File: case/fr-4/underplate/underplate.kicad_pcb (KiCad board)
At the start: 2 copper layers, 152.4 x 104.6 mm, 5 parts

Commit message: Fill all zones
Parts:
- added H6: Hole_Mount_M2, jiran-ble-lite:Hole_Mount_M2, F.Cu at (206.6, 106.2)
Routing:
- added copper zone on B.Cu, net (none)
- added copper zone on F.Cu, net (none)
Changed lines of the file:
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@@
       (drillshape 0)
       (scaleselection 1)
-      (outputdirectory "gerbers/")
+      (outputdirectory "D:/Git/jiran-ble-lite/case/fr-4/underplate/gerbers/")
     )
   )
   (net 0 "")
+  (footprint "jiran-ble-lite:Hole_Mount_M2" (layer "F.Cu")
+    (at 206.5782 106.2228)
+    (fp_text reference "H6" (at 0 0 unlocked) (layer "F.SilkS") hide
+      (effects (font (size 1 1) (thickness 0.15)))
+    )
+    (fp_text value "Hole_Mount_M2" (at 0 2.65 unlocked) (layer "F.Fab") hide
+      (effects (font (size 1 1) (thickness 0.15)))
+    )
+    (fp_circle (center 0 0) (end 1.5 0) (layer "Cmts.User") (width 0.12) (fill none))
+    (pad "" np_thru_hole circle (at 0 0) (size 2.1 2.1) (drill 2.1) (layers *.Cu *.Mask))
+  )
   (footprint "jiran-ble-lite:Hole_Mount_M2" (layer "F.Cu")
     (at 107.696 74.93)
@@
   (gr_arc (start 220.853 146.304) (end 220.853 147.447) (angle -90) (layer "Edge.Cuts") (width 0.1))
   (gr_arc (start 88.011 99.314) (end 87.376004 99.314) (angle 90) (layer "Edge.Cuts") (width 0.1))
+  (gr_line (start 204.089 147.447) (end 220.853 147.447) (layer "Edge.Cuts") (width 0.1))
   (gr_arc (start 127.889 48.768) (end 127.889 47.625) (angle -90) (layer "Edge.Cuts") (width 0.1))
   (gr_arc (start 106.553 55.88) (end 106.553 57.023) (angle -90) (layer "Edge.Cuts") (width 0.1))
@@
   (gr_arc (start 88.011 105.918004) (end 88.645996 105.918004) (angle 90) (layer "Edge.Cuts") (width 0.1))
   (gr_arc (start 201.803 146.304) (end 202.946 146.304) (angle -90) (layer "Edge.Cuts") (width 0.1))
-  (gr_line (start 220.853 147.447) (end 204.089 147.447) (layer "Edge.Cuts") (width 0.1))
   (gr_line (start 221.996 146.304) (end 221.996 54.864) (layer "Edge.Cuts") (width 0.1))
   (gr_line (start 108.839 54.737) (end 125.603 54.737) (layer "Edge.Cuts") (width 0.1))
   (gr_arc (start 125.603 129.794) (end 125.603 130.937) (angle -90) (layer "Edge.Cuts") (width 0.1))
   (gr_line (start 201.803 145.161) (end 185.039 145.161) (layer "Edge.Cuts") (width 0.1))
+  (zone (net 0) (net_name "") (layer "F.Cu") (hatch edge 0.508)
+    (connect_pads (clearance 0.508))
+    (min_thickness 0.254) (filled_areas_thickness no)
+    (fill yes (thermal_gap 0.508) (thermal_bridge_width 0.508))
+    (polygon
+      (pts
+        (xy 164.846 47.625)
+        (xy 183.896 47.625)
+        (xy 183.896 49.911)
+        (xy 202.946 49.911)
+        (xy 202.946 53.721)
+        (xy 221.996 53.721)
+        (xy 221.996 147.447)
+        (xy 202.946 147.447)
+        (xy 202.946 145.161)
+        (xy 183.896 145.161)
+        (xy 183.896 142.875)
+        (xy 164.846 142.875)
+        (xy 164.846 118.999)
+        (xy 145.796 118.999)
+        (xy 145.796 123.825)
+        (xy 126.746 123.825)
+        (xy 126.746 130.937)
+        (xy 107.696 130.937)
+        (xy 107.696 133.223)
+        (xy 88.646 133.223)
+        (xy 88.646 109.347)
+        (xy 69.596 109.347)
+        (xy 69.596 90.297)
+        (xy 88.646 90.297)
+        (xy 88.646 57.023)
+        (xy 107.696 57.023)
+        (xy 107.696 54.737)
+        (xy 126.746 54.737)
+        (xy 126.746 47.625)
+        (xy 145.796 47.625)
+        (xy 145.796 42.799)
+        (xy 164.846 42.799)
+      )
+    )
+  )
+  (zone (net 0) (net_name "") (layer "B.Cu") (hatch edge 0.508)
+    (connect_pads (clearance 0.508))
+    (min_thickness 0.254) (filled_areas_thickness no)
+    (fill yes (thermal_gap 0.508) (thermal_bridge_width 0.508))
+    (polygon
+      (pts
+        (xy 164.846 47.625)
+        (xy 183.896 47.625)
+        (xy 183.896 49.911)
+        (xy 202.946 49.911)
+        (xy 202.946 53.721)
+        (xy 221.996 53.721)
+        (xy 221.996 147.447)
+        (xy 202.946 147.447)
+        (xy 202.946 145.161)
+        (xy 183.896 145.161)
+        (xy 183.896 142.875)
+        (xy 164.846 142.875)
+        (xy 164.846 118.999)
+        (xy 145.796 118.999)
+        (xy 145.796 123.825)
+        (xy 126.746 123.825)
+        (xy 126.746 130.937)
+        (xy 107.696 130.937)
+        (xy 107.696 133.223)
+        (xy 88.646 133.223)
+        (xy 88.646 109.347)
+        (xy 69.596 109.347)
+        (xy 69.596 90.297)
+        (xy 88.646 90.297)
+        (xy 88.646 57.023)
+        (xy 107.696 57.023)
+        (xy 107.696 54.737)
+        (xy 126.746 54.737)
+        (xy 126.746 47.625)
+        (xy 145.796 47.625)
+        (xy 145.796 42.799)
+        (xy 164.846 42.799)
+      )
+    )
+  )
 )

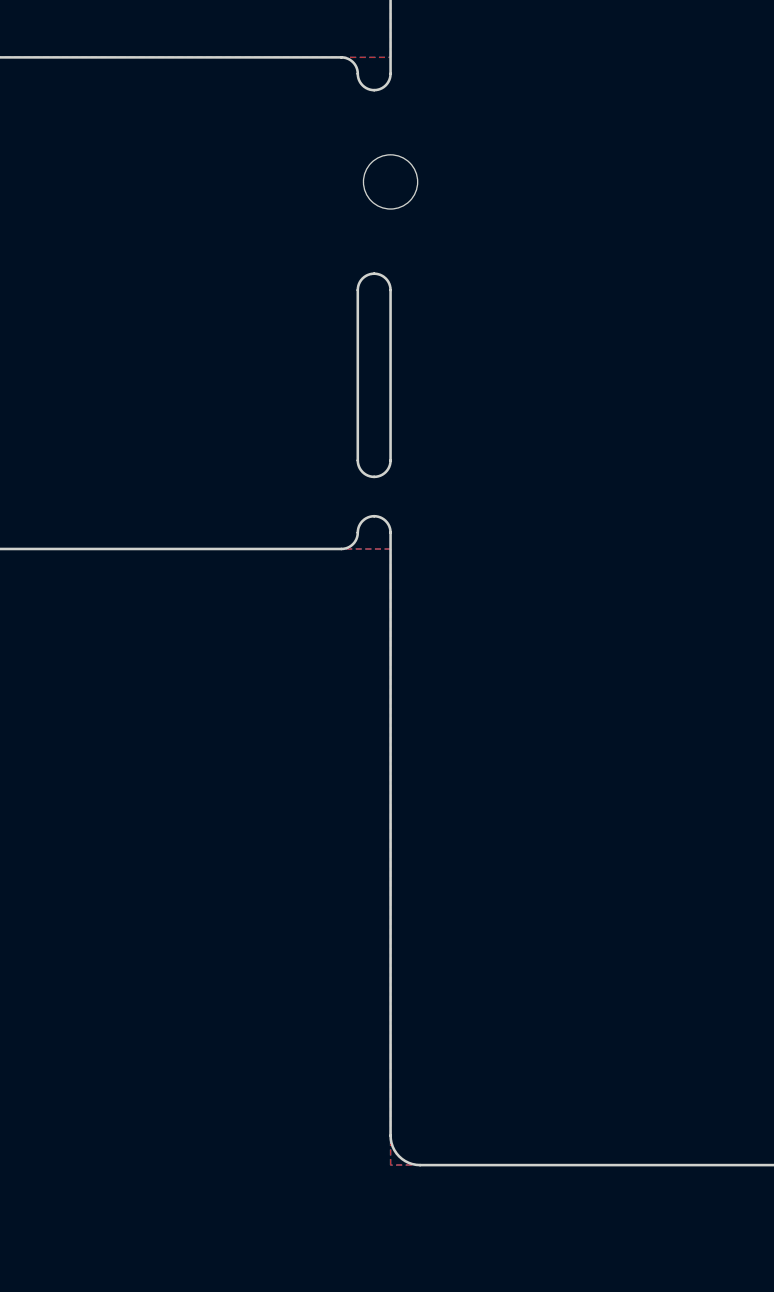
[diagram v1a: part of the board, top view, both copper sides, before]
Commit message: Edit cutout, re-fill zones
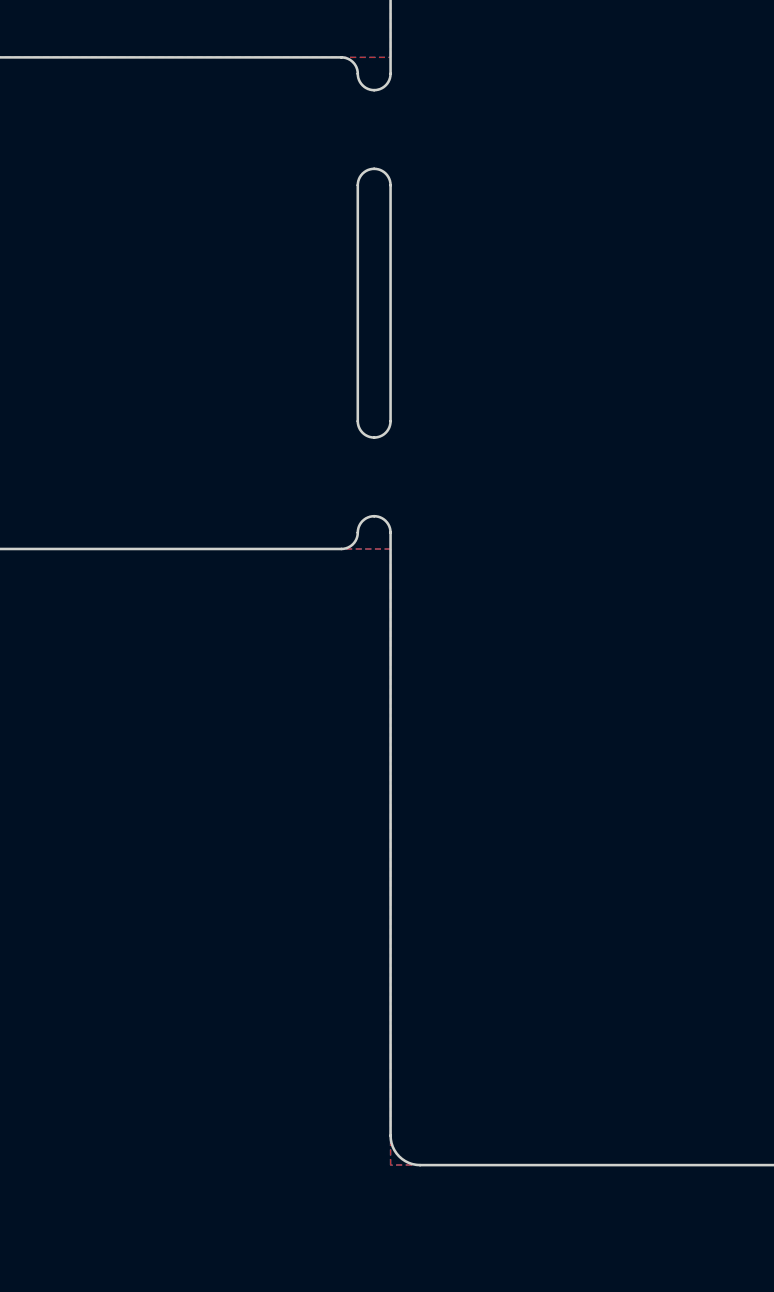
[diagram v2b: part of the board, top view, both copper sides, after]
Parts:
- removed H5: Hole_Mount_M2, jiran-ble-lite:Hole_Mount_M2
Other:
- outline, holes or cut-outs redrawn
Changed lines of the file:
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@@
-  )
-  (footprint "jiran-ble-lite:Hole_Mount_M2" (layer "F.Cu")
-    (at 88.646 95.123)
-    (fp_text reference "H5" (at 0 0 unlocked) (layer "F.SilkS") hide
-      (effects (font (size 1 1) (thickness 0.15)))
-    )
-    (fp_text value "Hole_Mount_M2" (at 0 2.65 unlocked) (layer "F.Fab") hide
-      (effects (font (size 1 1) (thickness 0.15)))
-    )
-    (fp_circle (center 0 0) (end 1.5 0) (layer "Cmts.User") (width 0.12) (fill none))
-    (pad "" np_thru_hole circle (at 0 0) (size 2.1 2.1) (drill 2.1) (layers *.Cu *.Mask))
   )
   (footprint "jiran-ble-lite:Hole_Mount_M2" (layer "F.Cu")
@@
     (pad "" np_thru_hole circle (at 0 0) (size 2.1 2.1) (drill 2.1) (layers *.Cu *.Mask))
   )
-  (gr_line (start 88.645996 105.918004) (end 88.645996 99.314) (layer "Edge.Cuts") (width 0.1))
   (gr_line (start 145.796 120.142) (end 145.796 122.682) (layer "Edge.Cuts") (width 0.1))
   (gr_line (start 145.796 46.482) (end 145.796 43.942) (layer "Edge.Cuts") (width 0.1))
-  (gr_arc (start 88.010993 90.931999) (end 88.645989 90.931999) (angle 90) (layer "Edge.Cuts") (width 0.1))
   (gr_arc (start 89.789 132.08) (end 88.646 132.08) (angle -90) (layer "Edge.Cuts") (width 0.1))
   (gr_line (start 127.889 47.625) (end 144.653 47.625) (layer "Edge.Cuts") (width 0.1))
   (gr_arc (start 165.989 141.732) (end 164.846 141.732) (angle -90) (layer "Edge.Cuts") (width 0.1))
-  (gr_line (start 88.646 58.166) (end 88.645989 90.931999) (layer "Edge.Cuts") (width 0.1))
+  (gr_line (start 88.645996 104.394004) (end 88.645996 95.249996) (layer "Edge.Cuts") (width 0.1))
   (gr_arc (start 185.039 144.018) (end 183.896 144.018) (angle -90) (layer "Edge.Cuts") (width 0.1))
   (gr_arc (start 146.939 43.942) (end 146.939 42.799) (angle -90) (layer "Edge.Cuts") (width 0.1))
   (gr_line (start 182.753 142.875) (end 165.989 142.875) (layer "Edge.Cuts") (width 0.1))
+  (gr_line (start 88.646 58.166) (end 88.645989 90.931999) (layer "Edge.Cuts") (width 0.1))
   (gr_line (start 202.946 51.054) (end 202.946 52.578) (layer "Edge.Cuts") (width 0.1))
-  (gr_arc (start 86.741 90.932) (end 86.741 90.297004) (angle 90) (layer "Edge.Cuts") (width 0.1))
   (gr_arc (start 163.703 43.942) (end 164.846 43.942) (angle -90) (layer "Edge.Cuts") (width 0.1))
   (gr_arc (start 127.889 124.968) (end 127.889 123.825) (angle -90) (layer "Edge.Cuts") (width 0.1))
   (gr_line (start 146.939 42.799) (end 163.703 42.799) (layer "Edge.Cuts") (width 0.1))
+  (gr_arc (start 88.010992 108.712004) (end 87.375996 108.712004) (angle 90) (layer "Edge.Cuts") (width 0.1))
   (gr_arc (start 220.853 54.864) (end 221.996 54.864) (angle -90) (layer "Edge.Cuts") (width 0.1))
   (gr_arc (start 182.753 48.768) (end 183.896 48.768) (angle -90) (layer "Edge.Cuts") (width 0.1))
@@
   (gr_line (start 70.739 90.297) (end 86.741 90.297004) (layer "Edge.Cuts") (width 0.1))
   (gr_arc (start 89.789 58.166) (end 89.789 57.023) (angle -90) (layer "Edge.Cuts") (width 0.1))
+  (gr_arc (start 86.741 108.712004) (end 87.375996 108.712004) (angle 90) (layer "Edge.Cuts") (width 0.1))
   (gr_line (start 164.846 141.732) (end 164.846 120.142) (layer "Edge.Cuts") (width 0.1))
   (gr_line (start 163.703 118.999) (end 146.939 118.999) (layer "Edge.Cuts") (width 0.1))
-  (gr_arc (start 88.010992 108.712004) (end 87.375996 108.712004) (angle 90) (layer "Edge.Cuts") (width 0.1))
+  (gr_line (start 87.376004 95.249996) (end 87.376004 104.394004) (layer "Edge.Cuts") (width 0.1))
+  (gr_arc (start 88.011 95.249996) (end 88.011 94.615) (angle 90) (layer "Edge.Cuts") (width 0.1))
   (gr_arc (start 220.853 146.304) (end 220.853 147.447) (angle -90) (layer "Edge.Cuts") (width 0.1))
-  (gr_arc (start 88.011 99.314) (end 87.376004 99.314) (angle 90) (layer "Edge.Cuts") (width 0.1))
+  (gr_arc (start 88.011 104.394004) (end 88.011 105.029) (angle 90) (layer "Edge.Cuts") (width 0.1))
   (gr_line (start 204.089 147.447) (end 220.853 147.447) (layer "Edge.Cuts") (width 0.1))
   (gr_arc (start 127.889 48.768) (end 127.889 47.625) (angle -90) (layer "Edge.Cuts") (width 0.1))
@@
   (gr_line (start 164.846 43.942) (end 164.846 46.482) (layer "Edge.Cuts") (width 0.1))
   (gr_line (start 165.989 47.625) (end 182.753 47.625) (layer "Edge.Cuts") (width 0.1))
+  (gr_arc (start 86.741 90.932) (end 86.741 90.297004) (angle 90) (layer "Edge.Cuts") (width 0.1))
+  (gr_line (start 88.645988 108.712004) (end 88.646 132.08) (layer "Edge.Cuts") (width 0.1))
   (gr_arc (start 165.989 46.482) (end 164.846 46.482) (angle -90) (layer "Edge.Cuts") (width 0.1))
-  (gr_arc (start 88.011 105.918004) (end 88.011 106.553) (angle 90) (layer "Edge.Cuts") (width 0.1))
+  (gr_arc (start 88.011 95.249996) (end 87.376004 95.249996) (angle 90) (layer "Edge.Cuts") (width 0.1))
+  (gr_arc (start 88.010992 108.712004) (end 88.010992 108.077008) (angle 90) (layer "Edge.Cuts") (width 0.1))
   (gr_arc (start 108.839 55.88) (end 108.839 54.737) (angle -90) (layer "Edge.Cuts") (width 0.1))
-  (gr_line (start 87.376004 99.314) (end 87.376004 105.918004) (layer "Edge.Cuts") (width 0.1))
   (gr_line (start 125.603 130.937) (end 108.839 130.937) (layer "Edge.Cuts") (width 0.1))
-  (gr_arc (start 88.011 99.314) (end 88.011 98.679004) (angle 90) (layer "Edge.Cuts") (width 0.1))
   (gr_line (start 69.596 108.204) (end 69.596 91.44) (layer "Edge.Cuts") (width 0.1))
   (gr_line (start 126.746 53.594) (end 126.746 48.768) (layer "Edge.Cuts") (width 0.1))
   (gr_arc (start 70.739 91.44) (end 70.739 90.297) (angle -90) (layer "Edge.Cuts") (width 0.1))
   (gr_line (start 144.653 123.825) (end 127.889 123.825) (layer "Edge.Cuts") (width 0.1))
-  (gr_arc (start 86.741 108.712004) (end 87.375996 108.712004) (angle 90) (layer "Edge.Cuts") (width 0.1))
-  (gr_line (start 88.646 132.08) (end 88.645987 108.712005) (layer "Edge.Cuts") (width 0.1))
   (gr_arc (start 201.803 51.054) (end 202.946 51.054) (angle -90) (layer "Edge.Cuts") (width 0.1))
   (gr_arc (start 70.739 108.204) (end 69.596 108.204) (angle -90) (layer "Edge.Cuts") (width 0.1))
@@
   (gr_line (start 106.553 133.223) (end 89.789 133.223) (layer "Edge.Cuts") (width 0.1))
   (gr_arc (start 204.089 146.304) (end 202.946 146.304) (angle -90) (layer "Edge.Cuts") (width 0.1))
-  (gr_arc (start 88.010991 108.712005) (end 88.010991 108.077009) (angle 90) (layer "Edge.Cuts") (width 0.1))
   (gr_arc (start 125.603 53.594) (end 125.603 54.737) (angle -90) (layer "Edge.Cuts") (width 0.1))
+  (gr_arc (start 88.010992 90.932) (end 88.010992 91.566996) (angle 90) (layer "Edge.Cuts") (width 0.1))
   (gr_arc (start 106.553 132.08) (end 106.553 133.223) (angle -90) (layer "Edge.Cuts") (width 0.1))
   (gr_arc (start 144.653 46.482) (end 144.653 47.625) (angle -90) (layer "Edge.Cuts") (width 0.1))
@@
   (gr_arc (start 144.653 122.682) (end 144.653 123.825) (angle -90) (layer "Edge.Cuts") (width 0.1))
   (gr_arc (start 182.753 144.018) (end 183.896 144.018) (angle -90) (layer "Edge.Cuts") (width 0.1))
-  (gr_arc (start 88.010992 90.932) (end 88.010992 91.566996) (angle 90) (layer "Edge.Cuts") (width 0.1))
-  (gr_arc (start 88.011 105.918004) (end 88.645996 105.918004) (angle 90) (layer "Edge.Cuts") (width 0.1))
+  (gr_arc (start 88.011 104.394004) (end 88.645996 104.394004) (angle 90) (layer "Edge.Cuts") (width 0.1))
   (gr_arc (start 201.803 146.304) (end 202.946 146.304) (angle -90) (layer "Edge.Cuts") (width 0.1))
   (gr_line (start 221.996 146.304) (end 221.996 54.864) (layer "Edge.Cuts") (width 0.1))
+  (gr_arc (start 88.010993 90.931999) (end 88.645989 90.931999) (angle 90) (layer "Edge.Cuts") (width 0.1))
   (gr_line (start 108.839 54.737) (end 125.603 54.737) (layer "Edge.Cuts") (width 0.1))
   (gr_arc (start 125.603 129.794) (end 125.603 130.937) (angle -90) (layer "Edge.Cuts") (width 0.1))
